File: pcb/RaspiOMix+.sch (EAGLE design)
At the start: 81 parts, among them IC1 MCP3424-E/SL, IC2 DS1307, IC4 MCP3424-E/SL, K1 PIN20X2, U1 EEPROM24

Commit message: Routage
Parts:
- removed IC1, IC4: MCP3424-E/SL, eagleParts:MCP3424-E/SL
- added C16, C17: 100nf, rcl:C-EUC0805
- added CON_IO_4, CON_IO_5, CON_IO_6, CON_IO_7: (no value), Seeedstudio_Connector:TWIG-4P-2.0
- added U$1, U$3: MCP3424-E/ST, eagleParts:MCP3424-E/ST
- renumbered C11 to CA4, C12 to CA5, C13 to CA6, C14 to CA7, C2 to CA0, C3 to CA1, C4 to CA2, C5 to CA3, R10 to RB7, R11 to RB6, R12 to RB5, R13 to RB4, R20 to RA0, R21 to RB0, R22 to RA1, R23 to RB1, R24 to RA2, R25 to RB2, R26 to RA3, R27 to RB3, R6 to RA7, R7 to RA6, R8 to RA5, R9 to RA4
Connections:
- new net IO4: CON_IO_3.2, CON_IO_4.1
- new net IO5: CON_IO_4.2, CON_IO_5.1
- new net IO6: CON_IO_5.2, CON_IO_6.1
- new net IO7: CON_IO_6.2, CON_IO_7.1
- new net N$13: U2.A1
- new net N$14: U2.A2
- new net N$15: U2.A3
- new net N$16: U2.A4
- new net N$17: U2.B1
- new net N$18: U2.B2
- new net N$19: U2.B3
- new net N$20: U2.B4
- net +3V3: now also C17.1, U$1.VDD, U$3.VDD, U2.OE, U2.VCCA; no longer IC1.VDD, IC4.VDD
- net +5V: now also C16.1, CON_IO_4.3, CON_IO_5.3, CON_IO_6.3, CON_IO_7.3, U2.VCCB
- net ADR0: now also U$1.ADR0, U$3.ADR0; no longer IC1.ADR0, IC4.ADR0
- net ADR1: now also U$1.ADR1, U$3.ADR1; no longer IC1.ADR1, IC4.ADR1
- net IO0: now also CON_IO_7.2; no longer CON_IO_3.2
- net N$10: now also U$3.CH2+; no longer IC4.CH2+
- net N$11: now also U$3.CH1+; no longer IC4.CH1+
- net N$4: now also U$1.CH4+; no longer IC1.CH4+
- net N$5: now also U$1.CH3+; no longer IC1.CH3+
- net N$6: now also U$1.CH2+; no longer IC1.CH2+
- net N$7: now also U$1.CH1+; no longer IC1.CH1+
- net N$8: now also U$3.CH4+; no longer IC4.CH4+
- net N$9: now also U$3.CH3+; no longer IC4.CH3+
- net PI_SCL: now also U$1.SCL, U$3.SCL; no longer IC1.SCL, IC4.SCL
- net PI_SDA: now also U$1.SDA, U$3.SDA; no longer IC1.SDA, IC4.SDA
- net VSS: now also C16.2, C17.2, CON_IO_4.4, CON_IO_5.4, CON_IO_6.4, CON_IO_7.4, U$1.CH1-, U$1.CH2-, U$1.CH3-, U$1.CH4-, U$1.VSS, U$3.CH1-, U$3.CH2-, U$3.CH3-, U$3.CH4-, U$3.VSS, U2.GND; no longer IC1.CH1-, IC1.CH2-, IC1.CH3-, IC1.CH4-, IC1.VSS, IC4.CH1-, IC4.CH2-, IC4.CH3-, IC4.CH4-, IC4.VSS
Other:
- moved on the sheet: C30, C31, CON_I2C_0, CON_I2C_1, CON_I2C_2, CON_IO_0, CON_IO_1, CON_IO_2, CON_IO_3, CON_SERIAL, IC3, U2

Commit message: Routage PCB
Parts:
- removed CR1220: (no value), adafruit:CR1220THM
- JP1: device jumper:JP1E -> FLYFISH:PIN2_100
- renumbered IO6 to IO??, U$1 to ICA0, U$3 to ICA1
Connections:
- net N$1 renamed ID_SC
- net N$2 renamed ID_SD
- removed net N$13: U2.A1
- removed net N$14: U2.A2
- removed net N$15: U2.A3
- removed net N$16: U2.A4
- removed net N$17: U2.B1
- removed net N$18: U2.B2
- removed net N$19: U2.B3
- removed net N$20: U2.B4
- new net ADR2: ICA1.ADR0, J_ADR3.2
- new net ADR3: ICA1.ADR1, J_ADR2.2
- new net PI_IO4: K1.35, U2.A1
- new net PI_IO5: K1.33, U2.A2
- new net PI_IO7: K1.29, U2.A4
- new net PI_IO??: K1.22
- net ADR0: no longer ICA1.ADR0, J_ADR3.2
- net ADR1: no longer ICA1.ADR1, J_ADR2.2
- net IO0: now also IC3.B4; no longer IC3.B1
- net IO1: now also IC3.B3; no longer IC3.B2
- net IO2: now also IC3.B2; no longer IC3.B3
- net IO3: now also IC3.B1; no longer IC3.B4
- net IO4: now also U2.B1
- net IO5: now also U2.B2
- net IO6: now also U2.B3
- net IO7: now also U2.B4
- net N$10: now also ICA1.CH1+; no longer ICA1.CH2+
- net N$11: now also ICA1.CH2+; no longer ICA1.CH1+
- net N$58: now also JP1.2; no longer CR1220.+, JP1.1
- net N$8: now also ICA1.CH3+; no longer ICA1.CH4+
- net N$9: now also ICA1.CH4+; no longer ICA1.CH3+
- net PI_DIP0: now also R5.2, SW1.3; no longer R4.2, SW1.4
- net PI_DIP1: now also R4.2, SW1.4; no longer R5.2, SW1.3
- net PI_IO0: now also IC3.A4; no longer IC3.A1
- net PI_IO1: now also IC3.A3; no longer IC3.A2
- net PI_IO2: now also IC3.A2; no longer IC3.A3
- net PI_IO3: now also IC3.A1; no longer IC3.A4
- net PI_IO6: now also K1.31, U2.A3; no longer IO??.TP, K1.22
- net PI_RX: now also IC3.A5; no longer IC3.A8
- net PI_SCL: now also IC3.A7; no longer IC3.A6
- net PI_SDA: now also IC3.A8; no longer IC3.A5
- net PI_TX: now also IC3.A6; no longer IC3.A7
- net RX: now also IC3.B5; no longer IC3.B8
- net SCL: now also IC3.B7; no longer IC3.B6
- net SDA: now also IC3.B8; no longer IC3.B5
- net TX: now also IC3.B6; no longer IC3.B7
- net VSS: now also JP1.1; no longer CR1220.-, JP1.2
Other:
- moved on the sheet: C1, CFG, K1, R1, R2, R3, U1

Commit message: RaspiO'Mix rev 1.0.0
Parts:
- removed C15: (no value), rcl:CPOL-EUB/3528-21R
- removed C16, C17, C28, C30, C31: 100nf, rcl:C-EUC0805
- removed ICA0, ICA1: MCP3424-E/ST, eagleParts:MCP3424-E/ST
- removed IO??: TPPAD1-13, testpad:TPPAD1-13
- removed R14: 330, rcl:R-EU_M0805
- removed R19: 1k, rcl:R-EU_M0805
- removed U2: (no value), adafruit:TXB0104PWR
- added C11, C12, C2, C4, C5: 100nf, rcl:C-EUC0805
- added C3: 100nF, resistor:C-EUC0805K
- added IC1: (no value), adafruit:TXB0108PWR
- added IC4, IC5: MCP3424-E/ST, eagleParts:MCP3424-E/ST
- added IC6: TMP101, tmp10x:TMP101
- added LOGO1: OSHW_LOGO_FILLX0350-NT, ohw-logo:OSHW_LOGO_FILLX0350-NT
- added R6, R7: 3k9, resistor:R-EU_M0805
- added TP10, TP11, TP12, TP2, TP3, TP4, TP5, TP6, TP7, TP8, TP9: TPTP12R, testpad:TPTP12R
- C1: value 100nF -> 220uf; device resistor:C-EUC0805K -> rcl:CPOL-EUD; DIELECTRIC X7R -> (none)
- C10: value 100nf -> (none); device rcl:C-EUC0805 -> rcl:CPOL-EUB/3528-21R
- C6: value (none) -> 100nf; device rcl:CPOL-EUB/3528-21R -> rcl:C-EUC0805
- C8: value 220uf -> (none); device rcl:CPOL-EUD -> rcl:CPOL-EUB/3528-21R
- C9: value 220uf -> 100nf; device rcl:CPOL-EUD -> rcl:C-EUC0805
- IC2: value DS1307 -> (none); device eagleParts:DS1307 -> adafruit:TXB0104PWR
- IC3: value (none) -> DS1307; device adafruit:TXB0108PWR -> eagleParts:DS1307
- R1: value 3k9 -> 330; device resistor:R-EU_M0805 -> rcl:R-EU_M0805; TOLERANCE 5% -> (none)
- R2: value 3k9 -> 10k; device resistor:R-EU_M0805 -> rcl:R-EU_M0805; TOLERANCE 5% -> (none)
- R3: value 1k -> 10k; device resistor:R-EU_M0805 -> rcl:R-EU_M0805; TOLERANCE 5% -> (none)
- R4: value 10k -> 1k
- R5: value 10k -> 1k; device rcl:R-EU_M0805 -> resistor:R-EU_M0805; TOLERANCE (none) -> 5%
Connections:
- removed net GND: C1.2
- removed net PI_CE0: K1.24
- removed net PI_CE1: K1.26
- removed net PI_IO??: K1.22
- removed net PI_MISO: K1.21
- removed net PI_MOSI: K1.19
- removed net PI_SCLK: K1.23
- new net N$1: K1.40, TP2.TP
- new net N$12: K1.36, TP4.TP
- new net N$13: K1.32, TP5.TP
- new net N$14: K1.37, TP6.TP
- new net N$15: K1.22, TP7.TP
- new net N$16: K1.24, TP8.TP
- new net N$17: K1.26, TP9.TP
- new net N$18: K1.19, TP10.TP
- new net N$19: K1.21, TP11.TP
- new net N$2: K1.38, TP3.TP
- new net N$20: K1.23, TP12.TP
- net +3V3: now also C10.+, C11.2, C12.1, C3.1, C4.1, C6.1, C8.+, C9.2, IC1.OE, IC1.VCCA, IC2.OE, IC2.VCCA, IC4.VDD, IC5.VDD, IC6.VCC, R4.2, R5.2, R6.2, R7.2; no longer C1.1, C10.2, C15.+, C17.1, C28.2, C30.1, C6.+, IC3.OE, IC3.VCCA, ICA0.VDD, ICA1.VDD, R1.2, R19.2, R2.2, R3.2, U2.OE, U2.VCCA
- net +5V: now also C1.+, C2.1, C5.1, IC1.VCCB, IC2.VCCB, IC3.VCC; no longer C16.1, C31.1, C8.+, C9.+, IC2.VCC, IC3.VCCB, U2.VCCB
- net ADR0: now also IC4.ADR0; no longer ICA0.ADR0
- net ADR1: now also IC4.ADR1; no longer ICA0.ADR1
- net ADR2: now also IC5.ADR0; no longer ICA1.ADR0
- net ADR3: now also IC5.ADR1; no longer ICA1.ADR1
- net ID_SC: now also R6.1; no longer R1.1
- net ID_SD: now also R7.1; no longer R2.1
- net INTC: now also IC3.SQW/OUT, R4.1; no longer IC2.SQW/OUT, R19.1
- net IO0: now also IC1.B4; no longer IC3.B4
- net IO1: now also IC1.B3; no longer IC3.B3
- net IO2: now also IC1.B2; no longer IC3.B2
- net IO3: now also IC1.B1; no longer IC3.B1
- net IO4: now also IC2.B1; no longer U2.B1
- net IO5: now also IC2.B2; no longer U2.B2
- net IO6: now also IC2.B3; no longer U2.B3
- net IO7: now also IC2.B4; no longer U2.B4
- net N$10: now also IC5.CH1+; no longer ICA1.CH1+
- net N$11: now also IC5.CH2+; no longer ICA1.CH2+
- net N$3: now also R5.1; no longer R3.1
- net N$33: now also IC3.X1; no longer IC2.X1
- net N$34: now also IC3.X2; no longer IC2.X2
- net N$39: now also R1.2; no longer R14.2
- net N$4: now also IC4.CH4+; no longer ICA0.CH4+
- net N$5: now also IC4.CH3+; no longer ICA0.CH3+
- net N$58: now also IC3.VBAT; no longer IC2.VBAT
- net N$6: now also IC4.CH2+; no longer ICA0.CH2+
- net N$7: now also IC4.CH1+; no longer ICA0.CH1+
- net N$8: now also IC5.CH3+; no longer ICA1.CH3+
- net N$9: now also IC5.CH4+; no longer ICA1.CH4+
- net PI_DIP0: now also R2.2, SW1.4; no longer R5.2, SW1.3
- net PI_DIP1: now also R3.2, SW1.3; no longer R4.2, SW1.4
- net PI_IO0: now also IC1.A4; no longer IC3.A4
- net PI_IO1: now also IC1.A3; no longer IC3.A3
- net PI_IO2: now also IC1.A2; no longer IC3.A2
- net PI_IO3: now also IC1.A1; no longer IC3.A1
- net PI_IO4: now also IC2.A1; no longer U2.A1
- net PI_IO5: now also IC2.A2; no longer U2.A2
- net PI_IO6: now also IC2.A3; no longer U2.A3
- net PI_IO7: now also IC2.A4; no longer U2.A4
- net PI_RX: now also IC1.A5; no longer IC3.A5
- net PI_SCL: now also IC1.A7, IC4.SCL, IC5.SCL, IC6.SCL; no longer IC3.A7, ICA0.SCL, ICA1.SCL
- net PI_SDA: now also IC1.A8, IC4.SDA, IC5.SDA, IC6.SDA; no longer IC3.A8, ICA0.SDA, ICA1.SDA
- net PI_TX: now also IC1.A6; no longer IC3.A6
- net RX: now also IC1.B5; no longer IC3.B5
- net SCL: now also IC1.B7, IC3.SCL; no longer IC2.SCL, IC3.B7
- net SDA: now also IC1.B8, IC3.SDA; no longer IC2.SDA, IC3.B8
- net TX: now also IC1.B6; no longer IC3.B6
- net VSS: now also C1.-, C10.-, C11.1, C12.2, C2.2, C3.2, C4.2, C5.2, C6.2, C9.1, IC1.GND, IC4.CH1-, IC4.CH2-, IC4.CH3-, IC4.CH4-, IC4.VSS, IC5.CH1-, IC5.CH2-, IC5.CH3-, IC5.CH4-, IC5.VSS, IC6.GND, R1.1, R2.1, R3.1; no longer C10.1, C15.-, C16.2, C17.2, C28.1, C30.2, C31.2, C6.-, C9.-, ICA0.CH1-, ICA0.CH2-, ICA0.CH3-, ICA0.CH4-, ICA0.VSS, ICA1.CH1-, ICA1.CH2-, ICA1.CH3-, ICA1.CH4-, ICA1.VSS, R14.1, R4.1, R5.1, U2.GND
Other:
- note added: "(optional)"
- note added: "Analog Digital Convertion"
- note added: "Temp"
- note removed: "ADC"
- note removed: "IO"
- moved on the sheet: C7, C8, CA0, CA1, CA2, CA3, CA4, CA5, CA6, CA7, CFG, CON_AN_0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

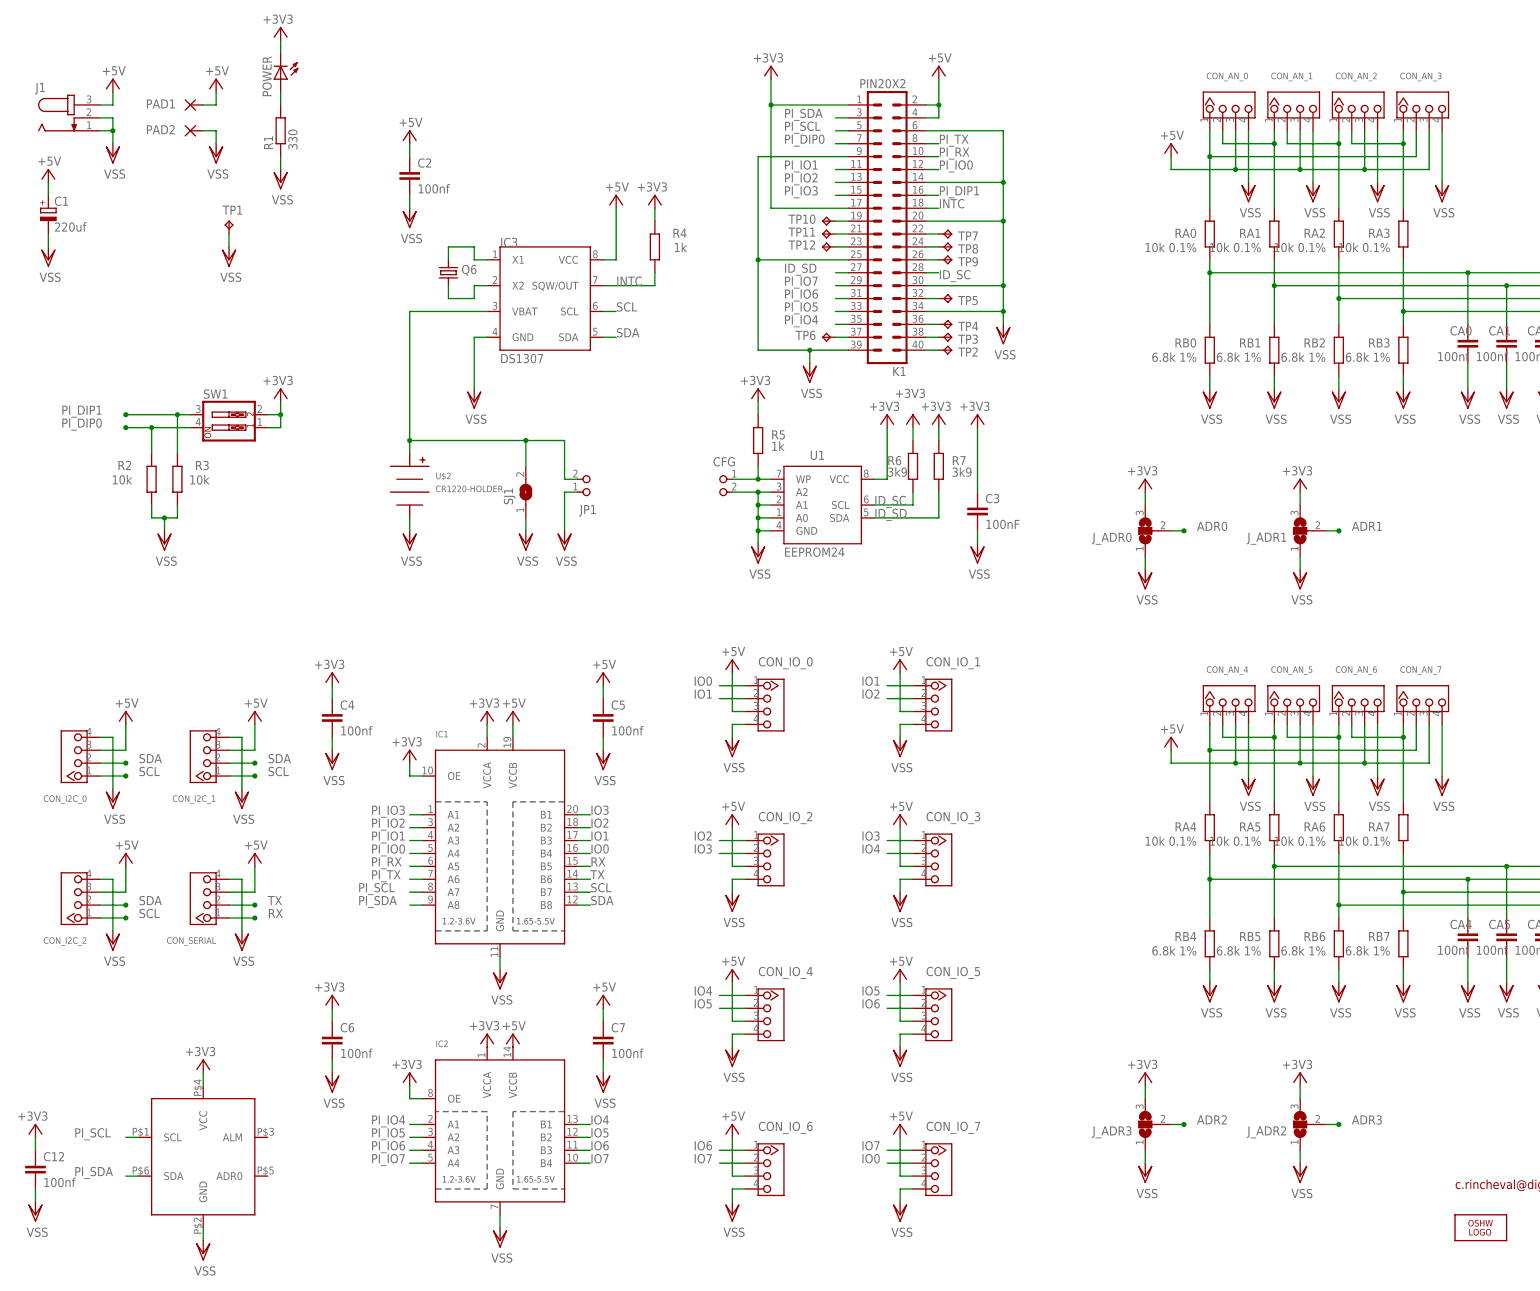
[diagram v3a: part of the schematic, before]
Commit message: RaspiO'Mix+
Modif
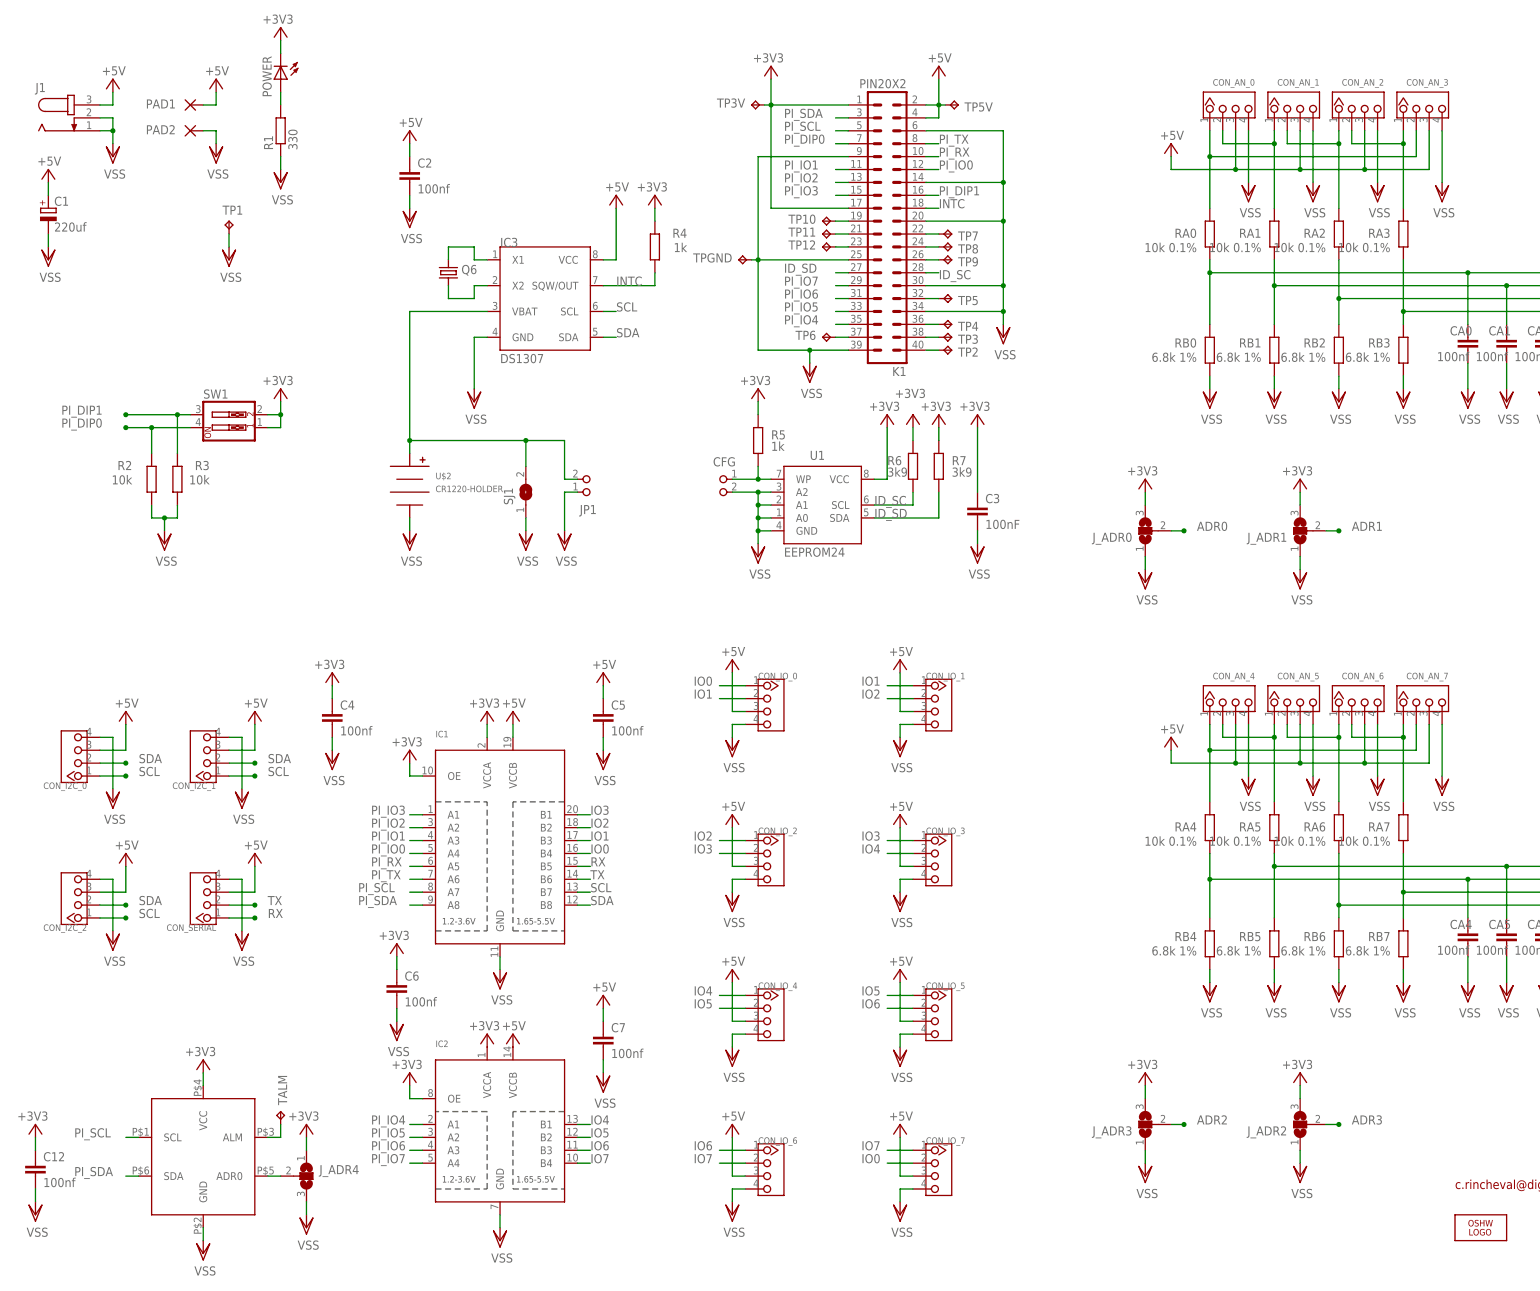
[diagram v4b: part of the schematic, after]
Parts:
- added J_ADR4: (no value), jumper:SJ2W
- added TALM, TP3V, TP5V, TPGND: TPTP12R, testpad:TPTP12R
- CON_AN_0, CON_AN_1, CON_AN_2, CON_AN_3, CON_AN_4, CON_AN_5, CON_AN_6, CON_AN_7, CON_I2C_0, CON_I2C_1, CON_I2C_2, CON_IO_0, CON_IO_1, CON_IO_2, CON_IO_3, CON_IO_4, CON_IO_5, CON_IO_6, CON_IO_7, CON_SERIAL: device Seeedstudio_Connector:TWIG-4P-2.0 -> Seeedstudio_Connector:TWIG-4P-2.0-2.0
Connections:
- new net N$21: IC6.ADR0, J_ADR4.2
- new net N$22: IC6.ALM, TALM.TP
- net +3V3: now also J_ADR4.1, TP3V.TP
- net +5V: now also TP5V.TP
- net VSS: now also J_ADR4.3, TPGND.TP
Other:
- moved on the sheet: C6
